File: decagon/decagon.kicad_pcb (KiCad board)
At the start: 2 copper layers, 153.8 x 161.7 mm, 39 parts, among them J1 Conn_01x05_Pin, J10 Conn_01x05_Pin, J2 Conn_01x05_Pin, J3 Conn_01x05_Pin, J4 Conn_01x05_Pin, J5 Conn_01x05_Pin, J6 Conn_01x05_Pin, J7 Conn_01x05_Pin, J8 Conn_01x05_Pin, J9 Conn_01x05_Pin

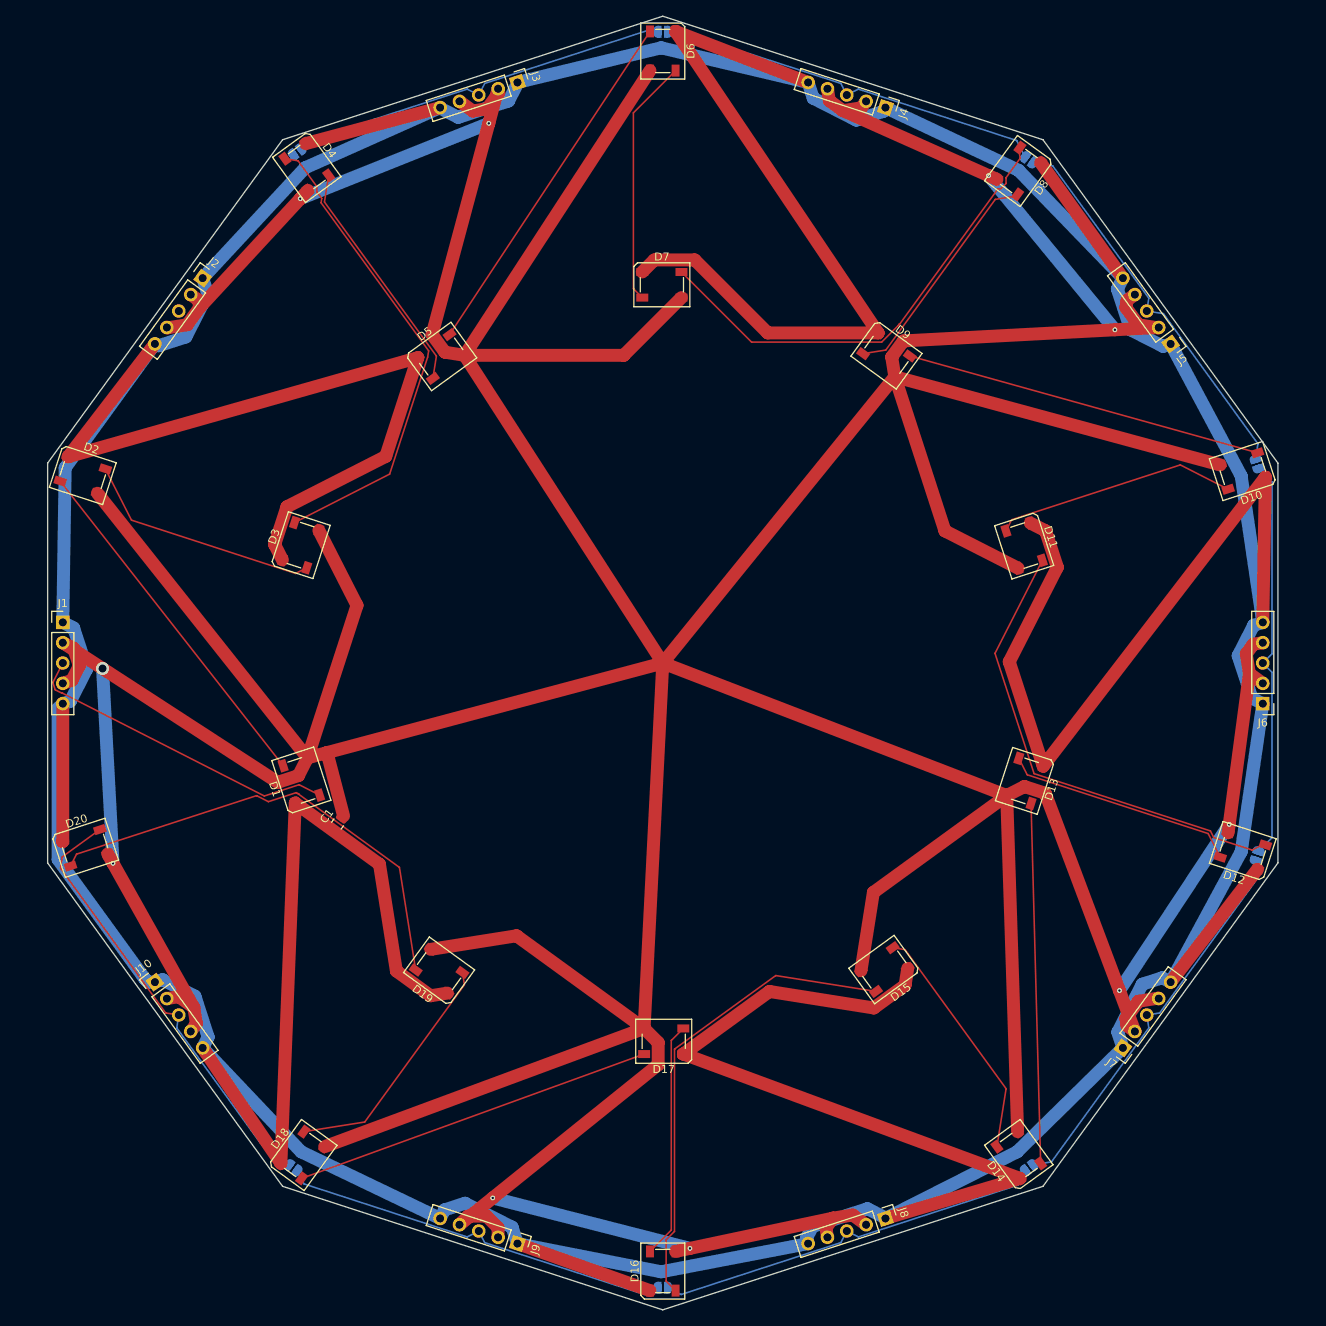
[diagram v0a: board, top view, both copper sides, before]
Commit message: fixed unconnected jumper wire
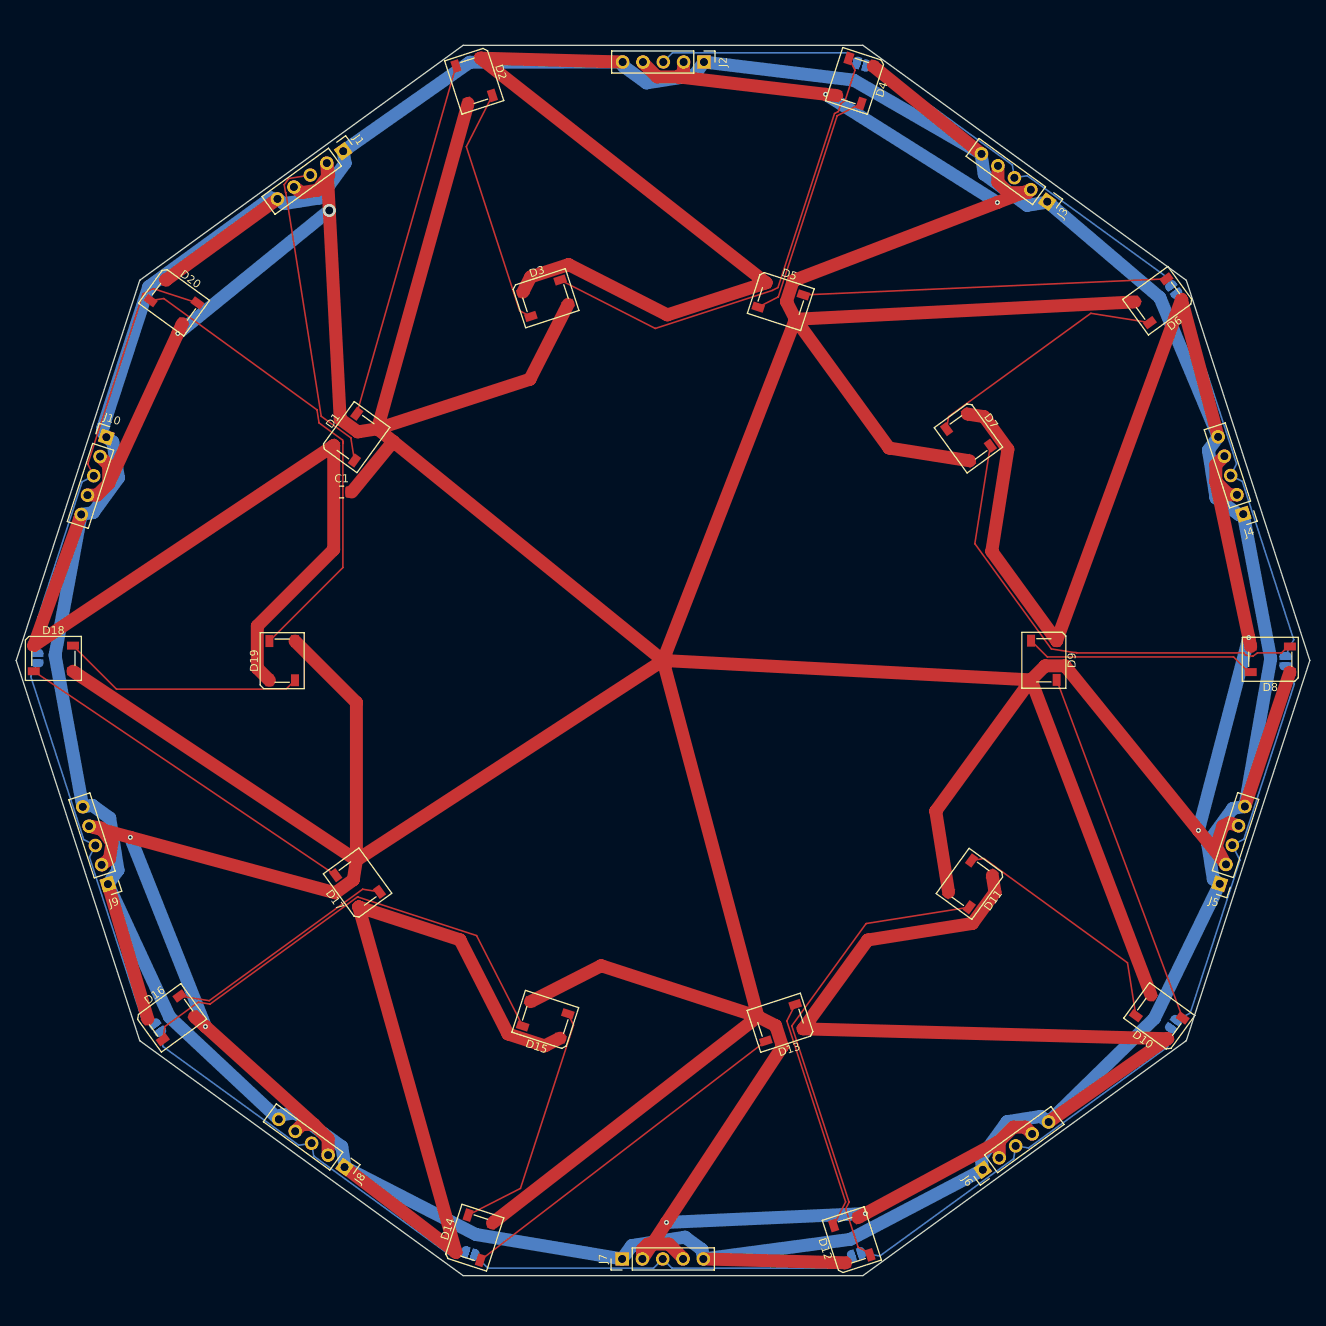
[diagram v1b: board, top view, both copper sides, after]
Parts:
- moved JP2 71.5 mm to (213.9, 53.7), turned to 126 degrees
- moved JP1 71.4 mm to (174.9, 25.6), turned to 162 degrees
- moved JP8 71.3 mm to (71.9, 99.8), turned to -90 degrees
- moved JP7 71.0 mm to (86.9, 146.0), turned to -54 degrees
- moved JP4 70.8 mm to (213.9, 145.6), turned to 54 degrees
- moved JP6 70.7 mm to (125.9, 174.2), turned to -18 degrees
- moved JP5 70.7 mm to (174.2, 174.4), turned to 18 degrees
- moved JP3 70.4 mm to (227.9, 100.2), turned to 90 degrees
- moved D18 69.5 mm to (73.9, 99.9), turned to 0 degrees
- moved D2 69.4 mm to (126.5, 27.6), turned to -72 degrees
- moved D4 69.4 mm to (174.1, 27.7), turned to -108 degrees
- moved D6 69.3 mm to (212.0, 55.1), turned to -144 degrees
- moved D20 69.1 mm to (88.9, 55.3), turned to -36 degrees
- moved D16 69.1 mm to (88.6, 144.8), turned to 36 degrees
- moved D10 69.0 mm to (212.1, 144.7), turned to 144 degrees
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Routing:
- net Net-(J2-Pin_3): track 0.00 -> 25.2 mm
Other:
- board size 153.8 x 161.7 mm -> 161.7 x 153.8 mm
